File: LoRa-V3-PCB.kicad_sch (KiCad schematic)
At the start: 85 parts, among them IC1 114993121, IC10 BR24G1MFVT-5AE2, IC11 BR24G1MFVT-5AE2, IC12 AEM00920, IC13 MCP73123T-22SI/MF, IC2 CP2102N-Axx-xQFN24, IC3 USBLC6-2P6, IC5 BME680, IC6 SHT40-BD1B-R2, IC7 TSL25911FN, IC8 BR24G1MFVT-5AE2, IC9 BR24G1MFVT-5AE2, Q1 PJC7400_R1_00001, Q2 Si2367DS, Q3 Si2367DS, Q4 Si2367DS, SW1 434331045822, SW2 SLLB510100

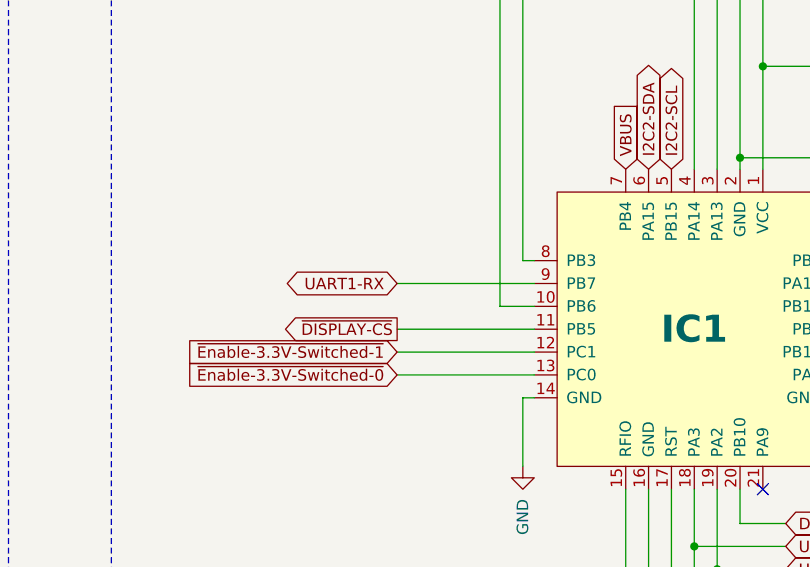
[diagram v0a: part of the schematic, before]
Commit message: fix DRC error
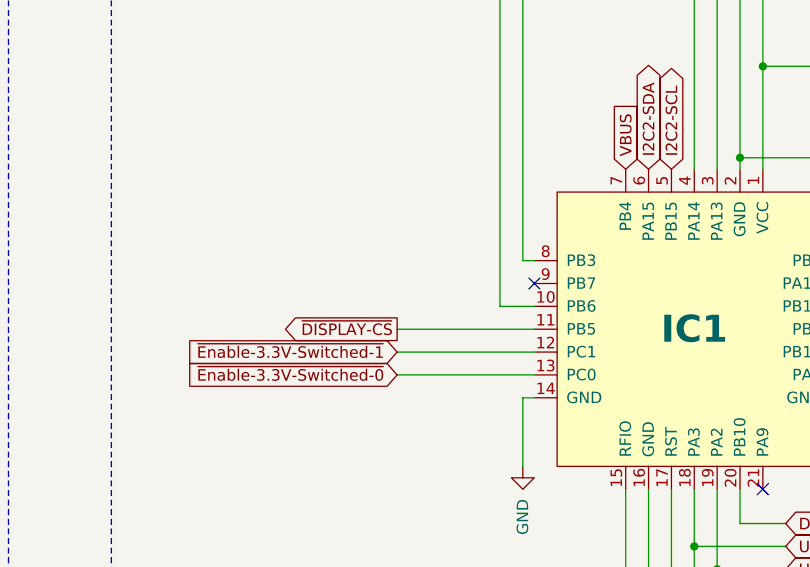
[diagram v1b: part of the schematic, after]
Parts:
- C1, C10, C11, C12, C13, C14, C15, C2, C20, C21, C22, C23, C24, C25, C3, C30, C31, C32, C33, C34, C35, C36, C37, C4, C5, C6, C7, C8: footprint 1GlobalFootprintsLibrary:C_0603_nominal -> 1projectLibrary:C_0603_nominal
- F1, F2, F3: footprint Fiducial:Fiducial_0.75mm_Mask1.5mm -> Fiducial:Fiducial_0.5mm_Mask1mm
- IC1: footprint 1GlobalFootprintsLibrary:LoRa-E5 -> 1projectLibrary:LoRa-E5; manufacturerPartNumber (none) -> 317990687; mouserPartNumber 713-114993121 -> 713-317990687
- IC13: manufacturerPartNumber (none) -> MCP73123T-22SI/MF
- R1, R10, R11, R12, R13, R14, R15, R16, R17, R18, R2, R3, R4, R5, R6, R7, R8, R9: footprint 1GlobalFootprintsLibrary:R_0603_nominal -> 1projectLibrary:R_0603_nominal
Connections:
- net UART1-RX: no longer names the net of IC1.9 (PB7)
- no-connect marks 30 -> 31

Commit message: bom fixes
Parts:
- C1, C2, C3, C4, C5, C6, C7, C8: GPN GPC0603104-25-X7R -> (none); MPN CGA3E2X7R1E104K080AA -> (none); digikeyPartNumber 445-5667-1-ND -> (none); genericPartNumber (none) -> GPC0603104-25-X7R; manufacturerPartNumber (none) -> CGA3E2X7R1E104K080AA; mouserPartNumber 810-CGA3E2X7R1E104K -> (none)
- C10, C11, C12, C13, C14, C15: GPN GPC0603475-10-X7S -> (none); MPN C1608X7S1A475K080AC -> (none); digikeyPartNumber 445-14258-1-ND -> (none); genericPartNumber (none) -> GPC0603475-10-X7S; manufacturerPartNumber (none) -> C1608X7S1A475K080AC; mouserPartNumber 810-C1608X7S1A475KAC -> (none)
- C20, C21, C23: MPN C0603C106M8PACTU -> (none); digikeyPartNumber 399-14945-1-ND -> (none); manufacturerPartNumber (none) -> C0603C106M8PACTU; mouserPartNumber 80-C0603C106M8PACTU -> (none)
- C22, C24, C25: GPN GPC0603475-10-X7S -> (none); MPN C0603C106M8PACTU -> (none); digikeyPartNumber 399-14945-1-ND -> (none); genericPartNumber (none) -> GPC0603475-10-X7S; manufacturerPartNumber (none) -> C0603C106M8PACTU; mouserPartNumber 80-C0603C106M8PACTU -> (none)
- C30, C31, C32, C33, C34, C35, C36, C37: GPN GPC0603105-25 -> (none); MPN CGA3E1X7R1E105K080AC -> (none); digikeyPartNumber 445-6931-1-ND -> (none); genericPartNumber (none) -> GPC0603105-25; manufacturerPartNumber (none) -> CGA3E1X7R1E105K080AC; mouserPartNumber 810-CGA3E1X7R1E105K -> (none)
- CONN1: MPN 217179-0001 -> (none); digikeyPartNumber 900-2171790001CT-ND -> (none); manufacturerPartNumber (none) -> 217179-0001; mouserPartNumber 538-217179-0001 -> (none)
- CONN2: MPN 1015 -> (none); digikeyPartNumber 36-1015-ND -> (none); manufacturerPartNumber (none) -> 1015; mouserPartNumber 534-1015 -> (none)
- CONN3, CONN4: MPN B2B-XH-A(LF)(SN) -> (none); digikeyPartNumber 455-2247-ND -> (none); manufacturerPartNumber (none) -> B2B-XH-A(LF)(SN); mouserPartNumber NA -> (none)
- CONN5: MPN 73391-0080 -> (none); digikeyPartNumber WM4088-ND -> (none); manufacturerPartNumber (none) -> 73391-0080; mouserPartNumber 538-73391-0080 -> (none)
- CONN6: MPN 2-1734839-4 -> (none); digikeyPartNumber A100299CT-ND -> (none); manufacturerPartNumber (none) -> 2-1734839-4; mouserPartNumber 571-2-1734839-4 -> (none)
- CONN7: MPN SM04B-SRSS-TB(LF)(DN)(P) -> (none); digikeyPartNumber 455-SM04B-SRSS-TBCT-ND -> (none); manufacturerPartNumber (none) -> SM04B-SRSS-TB(LF)(DN)(P); mouserPartNumber 306-SM04BSRSSTBLFDNP -> (none)
- CONN8, F1, F2, F3, H1, H2, H3, H4, JP1: MPN NA -> (none); manufacturerPartNumber (none) -> NA; mouserPartNumber NA -> (none)
- D1, D3: MPN MSS1P3HM3_A/H -> (none); digikeyPartNumber SDM05U40CSP-7DICT-ND -> (none); manufacturerPartNumber (none) -> MSS1P3HM3_A/H; mouserPartNumber MSS1P3HM3_A/H -> (none)
- D2: MPN MSS1P3HM3_A/H -> (none); digikeyPartNumber MSS1P3HM3_A/HGICT-ND -> (none); manufacturerPartNumber (none) -> MSS1P3HM3_A/H; mouserPartNumber MSS1P3HM3_A/H -> (none)
- IC1: MPN 114993121 -> (none); digikeyPartNumber 1597-114993121-ND -> (none); manufacturerPartNumber 317990687 -> 114993121; mouserPartNumber 713-317990687 -> (none)
- IC10, IC11, IC8, IC9: MPN BR24G1MFVT-5AE2 -> (none); digikeyPartNumber 846-BR24G1MFVT-5AE2CT-ND -> (none); manufacturerPartNumber (none) -> BR24G1MFVT-5AE2; mouserPartNumber 755-BR24G1MFVT-5AE2 -> (none)
- IC12: MPN AEM00920 -> (none); manufacturerPartNumber (none) -> AEM00920; mouserPartNumber NA -> (none)
- IC13: MPN MCP73123T-22SI/MF -> (none); digikeyPartNumber MCP73123T-22SI/MFCT-ND -> (none); mouserPartNumber 579-MCP73123T-22SIMF -> (none)
- IC2: MPN CP2102N-A02-GQFN24R -> (none); digikeyPartNumber 336-5888-1-ND -> (none); manufacturerPartNumber (none) -> CP2102N-A02-GQFN24R; mouserPartNumber 634-CP2102NA02QFN24R -> (none)
- IC3: MPN USBLC6-2P6 -> (none); digikeyPartNumber 497-5026-1-ND -> (none); manufacturerPartNumber (none) -> USBLC6-2P6; mouserPartNumber 511-USBLC6-2P6 -> (none)
- IC5: MPN BME680 -> (none); digikeyPartNumber 828-1077-1-ND -> (none); manufacturerPartNumber (none) -> BME680; mouserPartNumber 262-BME680 -> (none)
- IC6: MPN SHT40-BD1B-R2 -> (none); digikeyPartNumber 1649-SHT40-BD1B-R2CT-ND -> (none); manufacturerPartNumber (none) -> SHT40-BD1B-R2; mouserPartNumber 403-SHT40-AD1F-R2 -> (none)
- IC7: MPN TSL25911FN -> (none); digikeyPartNumber TSL25911FNCT-ND -> (none); manufacturerPartNumber (none) -> TSL25911FN; mouserPartNumber 985-TSL25911FN -> (none)
- L1: MPN VLS3010CX-470M-1 -> (none); digikeyPartNumber 445-VLS3010CX-470M-1CT-ND -> (none); manufacturerPartNumber (none) -> VLS3010CX-470M-1; mouserPartNumber 810-VLS3010CX470M1 -> (none)
- L2: MPN VLS3010CX-220M-1 -> (none); digikeyPartNumber 445-VLS3010CX-220M-1CT-ND -> (none); manufacturerPartNumber (none) -> VLS3010CX-220M-1; mouserPartNumber 810-VLS3010CX220M1 -> (none)
- Q1: MPN PJC7400_R1_00001 -> (none); digikeyPartNumber 3757-PJC7400_R1_00001CT-ND -> (none); manufacturerPartNumber (none) -> PJC7400_R1_00001; mouserPartNumber 241-PJC7400_R1_00001 -> (none)
- Q2, Q3, Q4: MPN SI2367DS-T1-GE3 -> (none); digikeyPartNumber SI2367DS-T1-GE3CT-ND -> (none); manufacturerPartNumber (none) -> SI2367DS-T1-GE3; mouserPartNumber 781-SI2367DS-GE3 -> (none)
- R1: GPN GPR06032R2 -> (none); MPN ERJ-3RQJ2R2V -> (none); digikeyPartNumber P2.2AHCT-ND -> (none); genericPartNumber (none) -> GPR06032R2; manufacturerPartNumber (none) -> ERJ-3RQJ2R2V; mouserPartNumber 667-ERJ-3RQJ2R2V -> (none)
- R10, R6, R7, R8, R9: GPN GPR06035K1 -> (none); MPN CR0603FX-5101ELF -> (none); digikeyPartNumber CR0603-FX-5101ELFCT-ND -> (none); genericPartNumber (none) -> GPR06035K1; manufacturerPartNumber (none) -> CR0603FX-5101ELF; mouserPartNumber 652-CR0603-FX-5101ELF -> (none)
- R11: MPN CR0603JW-752ELF -> (none); digikeyPartNumber CR0603-FX-7501ELFCT-ND -> (none); manufacturerPartNumber (none) -> CR0603JW-752ELF; mouserPartNumber 652-CR0603-FX-7501ELF -> (none)
- R12: GPN GPR060310K -> (none); MPN CR0603-JW-103ELF -> (none); digikeyPartNumber CR0603-FX-1002ELFCT-ND -> (none); genericPartNumber (none) -> GPR060310K; manufacturerPartNumber (none) -> CR0603-JW-103ELF; mouserPartNumber 652-CR0603-FX-1002ELF -> (none)
- R13: GPN GPR060322K1 -> (none); MPN CR0603FX-2212ELF -> (none); digikeyPartNumber CR0603-FX-2212ELFCT-ND -> (none); genericPartNumber (none) -> GPR060322K1; manufacturerPartNumber (none) -> CR0603FX-2212ELF; mouserPartNumber 652-CR0603-FX-2212ELF -> (none)
- R14: MPN CR0603FX-3752ELF -> (none); digikeyPartNumber 118-CR0603-FX-3742ELFCT-ND -> (none); manufacturerPartNumber (none) -> CR0603FX-3752ELF; mouserPartNumber 652-CR0603-FX-3742ELF -> (none)
- R15: GPN GPR060347K5 -> (none); MPN CR0603FX-4752ELF -> (none); digikeyPartNumber CR0603-FX-4752ELFCT-ND -> (none); genericPartNumber (none) -> GPR060347K5; manufacturerPartNumber (none) -> CR0603FX-4752ELF; mouserPartNumber 652-CR0603-FX-4752ELF -> (none)
- R16: MPN CR0603FX-2203ELF -> (none); digikeyPartNumber CR0603-FX-2203ELFCT-ND -> (none); manufacturerPartNumber (none) -> CR0603FX-2203ELF; mouserPartNumber 652-CR0603-FX-2203ELF -> (none)
- R17, R18: GPN GPR06031M -> (none); MPN CR0603-FX-1004ELF -> (none); digikeyPartNumber CR0603-FX-1004ELFCT-ND -> (none); genericPartNumber (none) -> GPR06031M; manufacturerPartNumber (none) -> CR0603-FX-1004ELF; mouserPartNumber 652-CR0603-FX-1004ELF -> (none)
- R2: MPN CR0603-FX-6800ELF -> (none); digikeyPartNumber CR0603-FX-6800ELFCT-ND -> (none); manufacturerPartNumber (none) -> CR0603-FX-6800ELF; mouserPartNumber 652-CR0603-FX-6800ELF -> (none)
- R3: GPN GPR06031K -> (none); MPN CR0603-JW-102ELF -> (none); digikeyPartNumber CR0603-FX-1001ELFCT-ND -> (none); genericPartNumber (none) -> GPR06031K; manufacturerPartNumber (none) -> CR0603-JW-102ELF; mouserPartNumber 652-CR0603-FX-1001ELF -> (none)
- R4, R5: MPN CR0603JW-332ELF -> (none); digikeyPartNumber CR0603-FX-3301ELFCT-ND -> (none); manufacturerPartNumber (none) -> CR0603JW-332ELF; mouserPartNumber 652-CR0603-FX-3301ELF -> (none)
- SW1: MPN 434331045822 -> (none); digikeyPartNumber 732-7055-1-ND -> (none); manufacturerPartNumber (none) -> 434331045822; mouserPartNumber 710-434331045822 -> (none)
- SW2: MPN SLLB510100 -> (none); digikeyPartNumber 4809-SLLB510100CT-ND -> (none); manufacturerPartNumber (none) -> SLLB510100; mouserPartNumber 688-SLLB510100 -> (none)

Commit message: bom cleanup
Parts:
- IC10, IC11, IC8, IC9: footprint 1GlobalFootprintsLibrary:BR24G1M-TSSOP-B8 -> thisProjectLibrary:TSSOP-B8; symbol 1GlobalSymbolsLibrary:BR24G1MFVT -> 1projectLibrary:BR24G1MFVT; digikeyPartNumber (none) -> 846-BR24G1MFVT-5AE2CT-ND; mouserPartNumber (none) -> 755-BR24G1MFVT-5AE2
- IC6: symbol 1GlobalSymbolsLibrary:SHT40 -> 1projectLibrary:SHT40
- Q2, Q3, Q4: footprint 1GlobalFootprintsLibrary:SI2367DS-SOT-23 -> 1projectLibrary:SI2367DS-SOT-23; symbol 1GlobalSymbolsLibrary:Si2367DS -> 1projectLibrary:Si2367DS
- SW1: symbol 1GlobalSymbolsLibrary:Switch_434331045822 -> 1projectLibrary:Switch_434331045822
- SW2: symbol 1GlobalSymbolsLibrary:SLLB510100 -> 1projectLibrary:SLLB510100
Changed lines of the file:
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@@
 	)
 	(symbol
-		(lib_id "1GlobalSymbolsLibrary:BR24G1MFVT")
+		(lib_id "1projectLibrary:BR24G1MFVT")
 		(at 232.41 372.11 0)
 		(unit 1)
@@
 			)
 		)
-		(property "Footprint" "1GlobalFootprintsLibrary:BR24G1M-TSSOP-B8"
+		(property "Footprint" "thisProjectLibrary:TSSOP-B8"
 			(at 232.41 394.97 0)
 			(effects
@@
 		)
 		(property "manufacturerPartNumber" "BR24G1MFVT-5AE2"
-			(at 232.41 372.11 0)
+			(at 232.41 410.21 0)
+			(effects
+				(font
+					(size 1.27 1.27)
+				)
+				(hide yes)
+			)
+		)
+		(property "mouserPartNumber" "755-BR24G1MFVT-5AE2"
+			(at 232.41 397.51 0)
+			(effects
+				(font
+					(size 1.27 1.27)
+				)
+				(hide yes)
+			)
+		)
+		(property "digikeyPartNumber" "846-BR24G1MFVT-5AE2CT-ND"
+			(at 232.41 405.13 0)
 			(effects
 				(font
@@
 	)
 	(symbol
-		(lib_id "1GlobalSymbolsLibrary:SLLB510100")
+		(lib_id "1projectLibrary:SLLB510100")
 		(at 392.43 48.26 0)
 		(unit 1)
@@
 	)
 	(symbol
-		(lib_id "1GlobalSymbolsLibrary:BR24G1MFVT")
+		(lib_id "1projectLibrary:BR24G1MFVT")
 		(at 265.43 372.11 0)
 		(unit 1)
@@
 			)
 		)
-		(property "Footprint" "1GlobalFootprintsLibrary:BR24G1M-TSSOP-B8"
+		(property "Footprint" "thisProjectLibrary:TSSOP-B8"
 			(at 265.43 394.97 0)
 			(effects
@@
 		)
 		(property "manufacturerPartNumber" "BR24G1MFVT-5AE2"
-			(at 265.43 372.11 0)
+			(at 265.43 410.21 0)
+			(effects
+				(font
+					(size 1.27 1.27)
+				)
+				(hide yes)
+			)
+		)
+		(property "mouserPartNumber" "755-BR24G1MFVT-5AE2"
+			(at 265.43 397.51 0)
+			(effects
+				(font
+					(size 1.27 1.27)
+				)
+				(hide yes)
+			)
+		)
+		(property "digikeyPartNumber" "846-BR24G1MFVT-5AE2CT-ND"
+			(at 265.43 405.13 0)
 			(effects
 				(font
@@
 	)
 	(symbol
-		(lib_id "1GlobalSymbolsLibrary:Si2367DS")
+		(lib_id "1projectLibrary:Si2367DS")
 		(at 500.38 53.34 0)
 		(unit 1)
@@
 			)
 		)
-		(property "Footprint" "1GlobalFootprintsLibrary:SI2367DS-SOT-23"
+		(property "Footprint" "1projectLibrary:SI2367DS-SOT-23"
 			(at 490.982 80.772 0)
 			(effects
@@
 		)
 		(property "manufacturerPartNumber" "SI2367DS-T1-GE3"
-			(at 500.38 53.34 0)
+			(at 500.38 60.452 0)
 			(effects
 				(font
@@
 	)
 	(symbol
-		(lib_id "1GlobalSymbolsLibrary:BR24G1MFVT")
+		(lib_id "1projectLibrary:BR24G1MFVT")
 		(at 299.72 372.11 0)
 		(unit 1)
@@
 			)
 		)
-		(property "Footprint" "1GlobalFootprintsLibrary:BR24G1M-TSSOP-B8"
+		(property "Footprint" "thisProjectLibrary:TSSOP-B8"
 			(at 299.72 394.97 0)
 			(effects
@@
 		)
 		(property "manufacturerPartNumber" "BR24G1MFVT-5AE2"
-			(at 299.72 372.11 0)
+			(at 299.72 410.21 0)
+			(effects
+				(font
+					(size 1.27 1.27)
+				)
+				(hide yes)
+			)
+		)
+		(property "mouserPartNumber" "755-BR24G1MFVT-5AE2"
+			(at 299.72 397.51 0)
+			(effects
+				(font
+					(size 1.27 1.27)
+				)
+				(hide yes)
+			)
+		)
+		(property "digikeyPartNumber" "846-BR24G1MFVT-5AE2CT-ND"
+			(at 299.72 405.13 0)
 			(effects
 				(font
@@
 		)
 		(property "Value" "TSL25911FN"
-			(at 102.87 386.08 0)
+			(at 105.41 381.508 0)
 			(effects
 				(font
@@
 		)
 		(property "Footprint" "1GlobalFootprintsLibrary:TSL2591"
-			(at 107.95 382.27 0)
+			(at 102.87 388.366 0)
 			(effects
 				(font
@@
 		)
 		(property "Description" "TSL25911"
-			(at 100.076 348.488 0)
+			(at 102.87 352.298 0)
 			(effects
 				(font
@@
 		)
 		(property "manufacturerName" "ams Osram"
-			(at 82.55 377.19 0)
+			(at 102.87 349.25 0)
 			(effects
 				(font
@@
 		)
 		(property "octopartUrl" "https://octopart.com/tsl25911fn-osram-126135547?r=sp"
-			(at 102.87 372.11 0)
+			(at 102.87 385.318 0)
 			(effects
 				(font
@@
 		)
 		(property "manufacturerPartNumber" "TSL25911FN"
-			(at 102.87 372.11 0)
+			(at 102.87 358.394 0)
 			(effects
 				(font
@@
 	)
 	(symbol
-		(lib_id "1GlobalSymbolsLibrary:BR24G1MFVT")
+		(lib_id "1projectLibrary:BR24G1MFVT")
 		(at 198.12 372.11 0)
 		(unit 1)
@@
 			)
 		)
-		(property "Footprint" "1GlobalFootprintsLibrary:BR24G1M-TSSOP-B8"
+		(property "Footprint" "thisProjectLibrary:TSSOP-B8"
 			(at 198.12 394.97 0)
 			(effects
@@
 		)
 		(property "manufacturerPartNumber" "BR24G1MFVT-5AE2"
-			(at 198.12 372.11 0)
+			(at 198.12 410.21 0)
+			(effects
+				(font
+					(size 1.27 1.27)
+				)
+				(hide yes)
+			)
+		)
+		(property "mouserPartNumber" "755-BR24G1MFVT-5AE2"
+			(at 198.12 397.51 0)
+			(effects
+				(font
+					(size 1.27 1.27)
+				)
+				(hide yes)
+			)
+		)
+		(property "digikeyPartNumber" "846-BR24G1MFVT-5AE2CT-ND"
+			(at 198.12 405.13 0)
 			(effects
 				(font
@@
 	)
 	(symbol
-		(lib_id "1GlobalSymbolsLibrary:SHT40")
+		(lib_id "1projectLibrary:SHT40")
 		(at 71.12 372.11 0)
 		(unit 1)
@@
 	)
 	(symbol
-		(lib_id "1GlobalSymbolsLibrary:Si2367DS")
+		(lib_id "1projectLibrary:Si2367DS")
 		(at 240.03 76.2 90)
 		(unit 1)
@@
 			)
 		)
-		(property "Footprint" "1GlobalFootprintsLibrary:SI2367DS-SOT-23"
+		(property "Footprint" "1projectLibrary:SI2367DS-SOT-23"
 			(at 267.462 85.598 0)
 			(effects
@@
 		)
 		(property "manufacturerPartNumber" "SI2367DS-T1-GE3"
-			(at 240.03 76.2 0)
+			(at 247.142 76.2 0)
 			(effects
 				(font
@@
 	)
 	(symbol
-		(lib_id "1GlobalSymbolsLibrary:Switch_434331045822")
+		(lib_id "1projectLibrary:Switch_434331045822")
 		(at 387.35 135.89 0)
 		(unit 1)
@@
 	)
 	(symbol
-		(lib_id "1GlobalSymbolsLibrary:Si2367DS")
+		(lib_id "1projectLibrary:Si2367DS")
 		(at 176.53 298.45 0)
 		(unit 1)
@@
 			)
 		)
-		(property "Footprint" "1GlobalFootprintsLibrary:SI2367DS-SOT-23"
+		(property "Footprint" "1projectLibrary:SI2367DS-SOT-23"
 			(at 167.132 325.882 0)
 			(effects
@@
 		)
 		(property "manufacturerPartNumber" "SI2367DS-T1-GE3"
-			(at 176.53 298.45 0)
+			(at 176.53 305.562 0)
 			(effects
 				(font

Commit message: fix bom
removing extra fields
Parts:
- IC10, IC11, IC8, IC9: digikeyPartNumber 846-BR24G1MFVT-5AE2CT-ND -> (none); mouserPartNumber 755-BR24G1MFVT-5AE2 -> (none); octopartUrl https://octopart.com/br24g1mfvt-5ae2-rohm-126430213?r=sp -> (none)
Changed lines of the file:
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@@
 			)
 		)
-		(property "octopartUrl" "https://octopart.com/br24g1mfvt-5ae2-rohm-126430213?r=sp"
-			(at 232.41 372.11 0)
-			(effects
-				(font
-					(size 1.27 1.27)
-				)
-				(hide yes)
-			)
-		)
 		(property "manufacturerPartNumber" "BR24G1MFVT-5AE2"
 			(at 232.41 410.21 0)
@@
 			)
 		)
-		(property "mouserPartNumber" "755-BR24G1MFVT-5AE2"
-			(at 232.41 397.51 0)
-			(effects
-				(font
-					(size 1.27 1.27)
-				)
-				(hide yes)
-			)
-		)
-		(property "digikeyPartNumber" "846-BR24G1MFVT-5AE2CT-ND"
-			(at 232.41 405.13 0)
-			(effects
-				(font
-					(size 1.27 1.27)
-				)
-				(hide yes)
-			)
-		)
 		(pin "1"
 		)
@@
 			)
 		)
-		(property "octopartUrl" "https://octopart.com/br24g1mfvt-5ae2-rohm-126430213?r=sp"
-			(at 265.43 372.11 0)
-			(effects
-				(font
-					(size 1.27 1.27)
-				)
-				(hide yes)
-			)
-		)
 		(property "manufacturerPartNumber" "BR24G1MFVT-5AE2"
 			(at 265.43 410.21 0)
@@
 			)
 		)
-		(property "mouserPartNumber" "755-BR24G1MFVT-5AE2"
-			(at 265.43 397.51 0)
-			(effects
-				(font
-					(size 1.27 1.27)
-				)
-				(hide yes)
-			)
-		)
-		(property "digikeyPartNumber" "846-BR24G1MFVT-5AE2CT-ND"
-			(at 265.43 405.13 0)
-			(effects
-				(font
-					(size 1.27 1.27)
-				)
-				(hide yes)
-			)
-		)
 		(pin "1"
 		)
@@
 			)
 		)
-		(property "octopartUrl" "https://octopart.com/br24g1mfvt-5ae2-rohm-126430213?r=sp"
-			(at 299.72 372.11 0)
-			(effects
-				(font
-					(size 1.27 1.27)
-				)
-				(hide yes)
-			)
-		)
 		(property "manufacturerPartNumber" "BR24G1MFVT-5AE2"
 			(at 299.72 410.21 0)
@@
 			)
 		)
-		(property "mouserPartNumber" "755-BR24G1MFVT-5AE2"
-			(at 299.72 397.51 0)
-			(effects
-				(font
-					(size 1.27 1.27)
-				)
-				(hide yes)
-			)
-		)
-		(property "digikeyPartNumber" "846-BR24G1MFVT-5AE2CT-ND"
-			(at 299.72 405.13 0)
-			(effects
-				(font
-					(size 1.27 1.27)
-				)
-				(hide yes)
-			)
-		)
 		(pin "5"
 		)
@@
 			)
 		)
-		(property "octopartUrl" "https://octopart.com/br24g1mfvt-5ae2-rohm-126430213?r=sp"
-			(at 198.12 372.11 0)
-			(effects
-				(font
-					(size 1.27 1.27)
-				)
-				(hide yes)
-			)
-		)
 		(property "manufacturerPartNumber" "BR24G1MFVT-5AE2"
 			(at 198.12 410.21 0)
 			(effects
 				(font
-					(size 1.27 1.27)
-				)
-				(hide yes)
-			)
-		)
-		(property "mouserPartNumber" "755-BR24G1MFVT-5AE2"
-			(at 198.12 397.51 0)
-			(effects
-				(font
-					(size 1.27 1.27)
-				)
-				(hide yes)
-			)
-		)
-		(property "digikeyPartNumber" "846-BR24G1MFVT-5AE2CT-ND"
-			(at 198.12 405.13 0)
-			(effects
-				(font
